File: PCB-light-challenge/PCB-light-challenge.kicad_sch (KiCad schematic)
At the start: 1 part

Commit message: RP2040  pinout toegevoegd   met naam
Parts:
- removed Schock-sens1: ~, symbol Light_challenge:Schock-sens
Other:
- removed sheet Force_sensor
- removed sheet Light_sensor
- added sheet Shock sens (Shock sens.kicad_sch)
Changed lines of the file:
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@@
 (kicad_sch (version 20230121) (generator eeschema)
   (paper "A4")
-  (rectangle (start 123.825 127) (end 160.02 146.05)
-    (stroke (width 0) (type default))
-    (fill (type none))
-  )
-  (symbol (lib_id "Light_challenge:Schock-sens") (at 141.605 132.08 0) (unit 1)
-    (in_bom yes) (on_board yes) (dnp no) (fields_autoplaced)
-    (property "Reference" "Schock-sens1" (at 142.24 130.81 0)
-      (effects (font (size 1.27 1.27)))
-    )
-    (property "Value" "~" (at 141.605 132.08 0)
-      (effects (font (size 1.27 1.27)))
-    )
-    (property "Footprint" "" (at 141.605 132.08 0)
-      (effects (font (size 1.27 1.27)) hide)
-    )
-    (property "Datasheet" "" (at 141.605 132.08 0)
-      (effects (font (size 1.27 1.27)) hide)
-    )
-    (pin "")
-    (pin "")
-    (pin "")
-    (pin "")
-    (instances
-      (project "PCB-light-challenge"
-        (path "/35573e8f-7834-430c-81d2-239f316c7834"
-          (reference "Schock-sens1") (unit 1)
-        )
-      )
-    )
-  )
   (sheet (at 38.1 25.4) (size 38.1 34.29) (fields_autoplaced)
     (stroke (width 0.1524) (type solid))
@@
     )
   )
-  (sheet (at 38.1 115.57) (size 40.64 21.59) (fields_autoplaced)
-    (stroke (width 0.1524) (type solid))
-    (fill (color 0 0 0 0.0000))
-    (property "Sheetname" "Light_sensor" (at 38.1 114.8584 0)
-      (effects (font (size 1.27 1.27)) (justify left bottom))
-    )
-    (property "Sheetfile" "Light_sensor.kicad_sch" (at 38.1 137.7446 0)
-      (effects (font (size 1.27 1.27)) (justify left top))
-    )
-    (instances
-      (project "PCB-light-challenge"
-        (path "/35573e8f-7834-430c-81d2-239f316c7834" (page "8"))
-      )
-    )
-  )
   (sheet (at 38.1 76.2) (size 39.37 26.67) (fields_autoplaced)
     (stroke (width 0.1524) (type solid))
@@
       (project "PCB-light-challenge"
         (path "/35573e8f-7834-430c-81d2-239f316c7834" (page "7"))
+      )
+    )
+  )
+  (sheet (at 40.005 120.65) (size 36.195 19.685) (fields_autoplaced)
+    (stroke (width 0.1524) (type solid))
+    (fill (color 0 0 0 0.0000))
+    (property "Sheetname" "Shock sens" (at 40.005 119.9384 0)
+      (effects (font (size 1.27 1.27)) (justify left bottom))
+    )
+    (property "Sheetfile" "Shock sens.kicad_sch" (at 40.005 140.9196 0)
+      (effects (font (size 1.27 1.27)) (justify left top))
+    )
+    (instances
+      (project "PCB-light-challenge"
+        (path "/35573e8f-7834-430c-81d2-239f316c7834" (page "10"))
       )
     )
@@
       (effects (font (size 1.27 1.27)) (justify left top))
     )
-    (instances
-      (project "PCB-light-challenge"
-        (path "/35573e8f-7834-430c-81d2-239f316c7834" (page "9"))
-      )
-    )
-  )
-  (sheet (at 38.1 146.05) (size 40.64 22.86) (fields_autoplaced)
-    (stroke (width 0.1524) (type solid))
-    (fill (color 0 0 0 0.0000))
-    (property "Sheetname" "Force_sensor" (at 38.1 145.3384 0)
-      (effects (font (size 1.27 1.27)) (justify left bottom))
-    )
-    (property "Sheetfile" "Force.kicad_sch" (at 38.1 169.4946 0)
-      (effects (font (size 1.27 1.27)) (justify left top))
-    )

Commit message: Footprints toegevoegd van alles
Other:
- removed sheet LEDS
- company: (none) -> HHS Living Labs
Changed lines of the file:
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@@
 (kicad_sch (version 20230121) (generator eeschema)
   (paper "A4")
-  (sheet (at 38.1 25.4) (size 38.1 34.29) (fields_autoplaced)
-    (stroke (width 0.1524) (type solid))
-    (fill (color 0 0 0 0.0000))
-    (property "Sheetname" "LEDS" (at 38.1 24.6884 0)
-      (effects (font (size 1.27 1.27)) (justify left bottom))
-    )
-    (property "Sheetfile" "LEDS.kicad_sch" (at 38.1 60.2746 0)
-      (effects (font (size 1.27 1.27)) (justify left top))
-    )
-    (instances
-      (project "PCB-light-challenge"
-        (path "/35573e8f-7834-430c-81d2-239f316c7834" (page "6"))
-      )
-    )
+  (title_block
+    (date "2023-11-06")
+    (rev "V0.1")
+    (company "HHS Living Labs")
   )
   (sheet (at 200.66 76.2) (size 38.1 30.48) (fields_autoplaced)

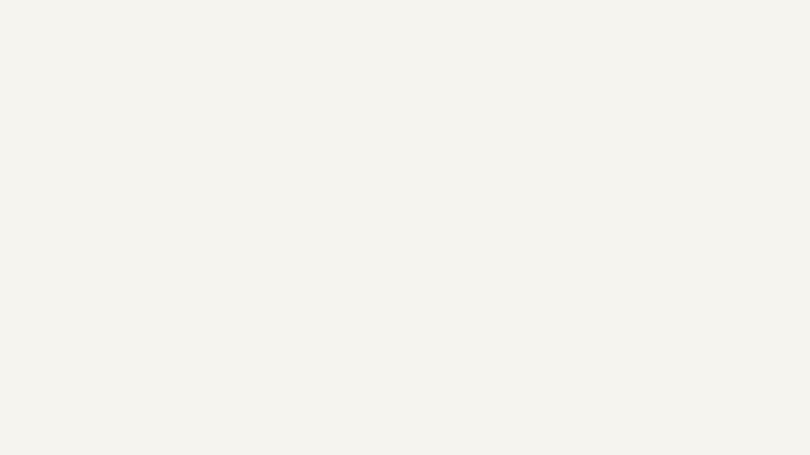
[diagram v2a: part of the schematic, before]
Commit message: TP footprint verandert,  apparte grond (P-) gemaakt.  AC  clearance verandert.  connector voor PIR verandert
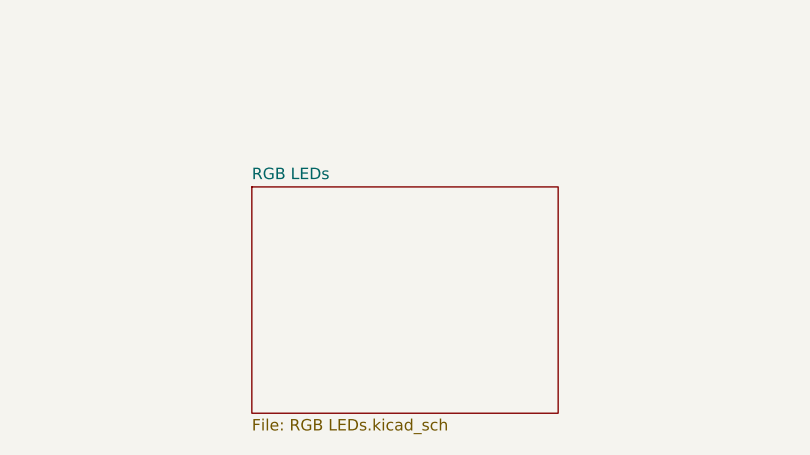
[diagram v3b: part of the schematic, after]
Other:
- added sheet RGB LEDs (RGB LEDs.kicad_sch)
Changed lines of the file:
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@@
+    )
+  )
+  (sheet (at 109.474 138.43) (size 34.036 25.146) (fields_autoplaced)
+    (stroke (width 0.1524) (type solid))
+    (fill (color 0 0 0 0.0000))
+    (property "Sheetname" "RGB LEDs" (at 109.474 137.7184 0)
+      (effects (font (size 1.27 1.27)) (justify left bottom))
+    )
+    (property "Sheetfile" "RGB LEDs.kicad_sch" (at 109.474 164.1606 0)
+      (effects (font (size 1.27 1.27)) (justify left top))
+    )
+    (instances
+      (project "PCB-light-challenge"
+        (path "/35573e8f-7834-430c-81d2-239f316c7834" (page "8"))
+      )
     )
   )

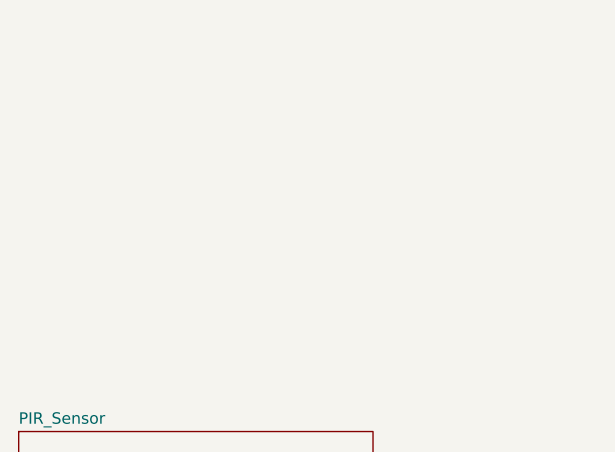
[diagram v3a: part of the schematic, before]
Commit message: Vias  kleiner gemaakt en grond GND genoemd op silkscreen
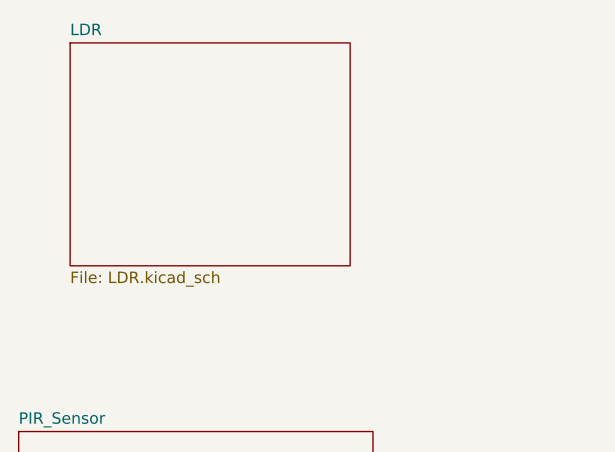
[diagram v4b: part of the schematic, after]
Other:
- added sheet LDR (LDR.kicad_sch)
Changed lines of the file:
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@@
+    )
+  )
+  (sheet (at 43.815 33.02) (size 31.115 24.765) (fields_autoplaced)
+    (stroke (width 0.1524) (type solid))
+    (fill (color 0 0 0 0.0000))
+    (property "Sheetname" "LDR" (at 43.815 32.3084 0)
+      (effects (font (size 1.27 1.27)) (justify left bottom))
+    )
+    (property "Sheetfile" "LDR.kicad_sch" (at 43.815 58.3696 0)
+      (effects (font (size 1.27 1.27)) (justify left top))
+    )
+    (instances
+      (project "PCB-light-challenge"
+        (path "/35573e8f-7834-430c-81d2-239f316c7834" (page "9"))
+      )
     )
   )
